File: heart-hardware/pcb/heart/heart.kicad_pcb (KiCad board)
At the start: 4 copper layers, 47.6 x 45.2 mm, 68 parts, among them J1 3V0, J2 DIO, J3 CLK, J4 GND, J5 TOUCH_KEY, SW1 SW_SPDT, U1 STM32L031F6Px, U2 TCA6416APWR, U3 LIS3DH, U4 Holtek-Semicon-BS812A-1

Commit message: Version 1.0
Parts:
- renumbered JP3 to RST
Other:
- board text added: "github/lime7git"
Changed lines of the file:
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@@
   (general
     (thickness 1.6)
-    (drawings 41)
+    (drawings 42)
     (tracks 464)
     (zones 0)
@@
     (1 In1.Cu signal)
     (2 In2.Cu signal)
-    (31 B.Cu signal)
+    (31 B.Cu signal hide)
     (32 B.Adhes user)
     (33 F.Adhes user)
@@
     (tags "solder jumper open")
     (attr virtual)
-    (fp_text reference JP3 (at -2.75 -0.01) (layer B.SilkS)
+    (fp_text reference RST (at -2.75 -0.01) (layer B.SilkS)
       (effects (font (size 1 1) (thickness 0.15)) (justify mirror))
     )
@@
       ))
   )
+  (gr_text github/lime7git (at 50 98) (layer B.SilkS)
+    (effects (font (size 0.5 0.5) (thickness 0.1)) (justify mirror))
+  )
   (gr_arc (start 50.006349 60.288693) (end 52.636348 59.968694) (angle 194.5) (layer B.SilkS) (width 0.2))

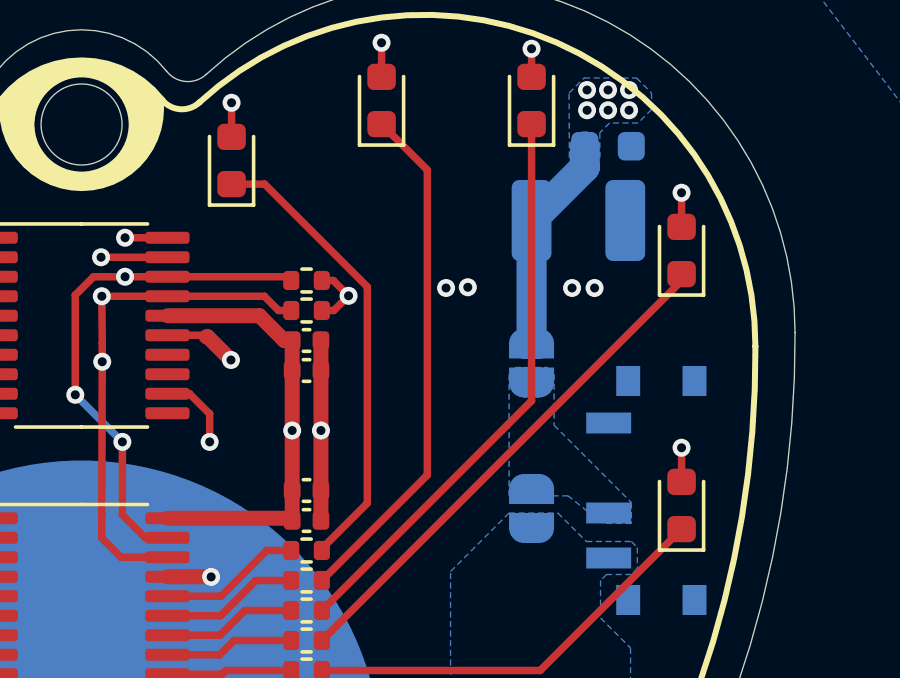
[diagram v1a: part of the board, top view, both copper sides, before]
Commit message: Version 1.01, change power planes clearance
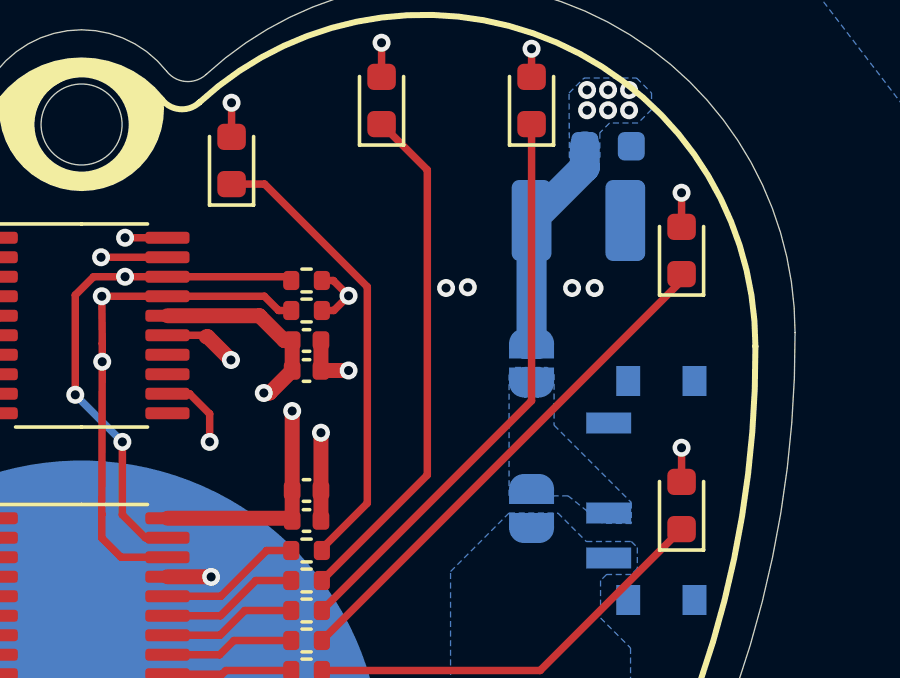
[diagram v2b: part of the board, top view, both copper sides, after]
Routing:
- net GND: track 32.9 -> 31.7 mm, vias 15 -> 16
- net +3V0: track 86.3 -> 86.2 mm, vias 30 -> 31
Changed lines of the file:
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@@
     (thickness 1.6)
     (drawings 42)
-    (tracks 464)
+    (tracks 467)
     (zones 0)
     (modules 68)
@@
     (1 In1.Cu signal)
     (2 In2.Cu signal)
-    (31 B.Cu signal hide)
+    (31 B.Cu signal)
     (32 B.Adhes user)
     (33 F.Adhes user)
@@
     (user_trace_width 1)
     (trace_clearance 0.2)
-    (zone_clearance 0.508)
+    (zone_clearance 0.254)
     (zone_45_only no)
     (trace_min 0.2)
@@
       (outputformat 1)
       (mirror false)
-      (drillshape 1)
+      (drillshape 0)
       (scaleselection 1)
-      (outputdirectory ""))
+      (outputdirectory "../../production-files/"))
   )
   (net 0 "")
@@
       (effects (font (size 1 1) (thickness 0.15)))
     )
-    (fp_text user %R (at 0 0) (layer F.Fab)
-      (effects (font (size 0.75 0.75) (thickness 0.11)))
-    )
     (fp_line (start 0.935 -1.61) (end 1.61 -1.61) (layer F.SilkS) (width 0.12))
     (fp_line (start 1.61 -1.61) (end 1.61 -1.435) (layer F.SilkS) (width 0.12))
@@
     (fp_line (start 1.75 1.75) (end 1.75 -1.75) (layer F.CrtYd) (width 0.05))
     (fp_line (start 1.75 -1.75) (end -1.75 -1.75) (layer F.CrtYd) (width 0.05))
+    (fp_text user %R (at 0 0) (layer F.Fab)
+      (effects (font (size 0.75 0.75) (thickness 0.11)))
+    )
     (pad 16 smd roundrect (at -0.5 -1.225) (size 0.35 0.55) (layers F.Cu F.Paste F.Mask) (roundrect_rratio 0.25)
       (net 37 "Net-(U3-Pad16)"))
@@
       (effects (font (size 0.8 0.8) (thickness 0.12)) (justify mirror))
     )
-    (pad 2 smd roundrect (at 1.5625 0) (size 1.325 2.7) (layers B.Cu B.Paste B.Mask) (roundrect_rratio 0.188679)
+    (pad 2 smd roundrect (at 1.5625 0) (size 1.325 2.7) (layers B.Cu B.Paste B.Mask) (roundrect_rratio 0.1886784905660377)
       (net 2 GND))
-    (pad 1 smd roundrect (at -1.5625 0) (size 1.325 2.7) (layers B.Cu B.Paste B.Mask) (roundrect_rratio 0.188679)
+    (pad 1 smd roundrect (at -1.5625 0) (size 1.325 2.7) (layers B.Cu B.Paste B.Mask) (roundrect_rratio 0.1886784905660377)
       (net 3 +3V0))
     (model ${KISYS3DMOD}/Capacitor_SMD.3dshapes/C_1210_3225Metric.wrl
@@
     (effects (font (size 2.900172 2.610154) (thickness 0.362521)) (justify left top))
   )
+  (via (at 58.9 69) (size 0.6) (drill 0.3) (layers F.Cu B.Cu) (net 2))
+  (via (at 56.075 69.75) (size 0.6) (drill 0.3) (layers F.Cu B.Cu) (net 3))
   (via (at 44.725 85.5) (size 0.6) (drill 0.3) (layers F.Cu B.Cu) (net 2))
-  (via (at 32.175 66.675) (size 0.6) (drill 0.3) (layers F.Cu B.Cu) (net 3))
-  (via (at 66.85 60.325) (size 0.6) (drill 0.3) (layers F.Cu B.Cu) (net 3))
-  (via (at 67.55 60.325) (size 0.6) (drill 0.3) (layers F.Cu B.Cu) (net 3))
-  (via (at 68.25 60.325) (size 0.6) (drill 0.3) (layers F.Cu B.Cu) (net 3))
-  (via (at 68.25 59.65) (size 0.6) (drill 0.3) (layers F.Cu B.Cu) (net 3))
-  (via (at 67.55 59.65) (size 0.6) (drill 0.3) (layers F.Cu B.Cu) (net 3))
-  (via (at 66.85 59.65) (size 0.6) (drill 0.3) (layers F.Cu B.Cu) (net 3))
   (via (at 45.5 81.5) (size 0.6) (drill 0.3) (layers F.Cu B.Cu) (net 2))
   (via (at 54.32 75.88) (size 0.6) (drill 0.3) (layers F.Cu B.Cu) (net 2))
   (via (at 42.02 68.1) (size 0.6) (drill 0.3) (layers F.Cu B.Cu) (net 2))
   (via (at 54.98 68.65) (size 0.6) (drill 0.3) (layers F.Cu B.Cu) (net 2))
-  (via (at 57.98 71) (size 0.6) (drill 0.3) (layers F.Cu B.Cu) (net 2))
+  (via (at 57.98 71.075) (size 0.6) (drill 0.3) (layers F.Cu B.Cu) (net 2))
   (segment (start 52.8675 67.82) (end 52.8625 67.825) (width 0.25) (layer F.Cu) (net 2))
   (segment (start 52.8675 75.88) (end 52.8625 75.875) (width 0.25) (layer F.Cu) (net 2))
@@
   (segment (start 48.775 86) (end 48.775 87.035) (width 0.25) (layer F.Cu) (net 2))
   (segment (start 57.98 68) (end 57.98 69) (width 0.5) (layer F.Cu) (net 2))
-  (segment (start 57.98 71) (end 57.98 69) (width 0.5) (layer F.Cu) (net 2))
-  (segment (start 57.98 71) (end 57.98 73) (width 0.5) (layer F.Cu) (net 2))
   (segment (start 41.99 65.175) (end 41.99 66.145) (width 0.5) (layer F.Cu) (net 2))
   (segment (start 42.02 66.175) (end 41.99 66.145) (width 0.5) (layer F.Cu) (net 2))
@@
   (segment (start 54.20501 67.87501) (end 54.155 67.87501) (width 0.5) (layer F.Cu) (net 2))
   (segment (start 54.98 68.65) (end 54.20501 67.87501) (width 0.5) (layer F.Cu) (net 2))
+  (segment (start 57.98 73) (end 57.98 71.075) (width 0.5) (layer F.Cu) (net 2))
+  (segment (start 58.9 69) (end 57.98 69) (width 0.5) (layer F.Cu) (net 2))
+  (via (at 32.175 66.675) (size 0.6) (drill 0.3) (layers F.Cu B.Cu) (net 3))
+  (via (at 66.85 60.325) (size 0.6) (drill 0.3) (layers F.Cu B.Cu) (net 3))
+  (via (at 67.55 60.325) (size 0.6) (drill 0.3) (layers F.Cu B.Cu) (net 3))
+  (via (at 68.25 60.325) (size 0.6) (drill 0.3) (layers F.Cu B.Cu) (net 3))
+  (via (at 68.25 59.65) (size 0.6) (drill 0.3) (layers F.Cu B.Cu) (net 3))
+  (via (at 67.55 59.65) (size 0.6) (drill 0.3) (layers F.Cu B.Cu) (net 3))
+  (via (at 66.85 59.65) (size 0.6) (drill 0.3) (layers F.Cu B.Cu) (net 3))
   (via (at 55 60.075) (size 0.6) (drill 0.3) (layers F.Cu B.Cu) (net 3))
   (via (at 60 58.075) (size 0.6) (drill 0.3) (layers F.Cu B.Cu) (net 3))
@@
   (via (at 69.25 81.7) (size 0.6) (drill 0.3) (layers F.Cu B.Cu) (net 3))
   (via (at 43.175 68.1) (size 0.6) (drill 0.3) (layers F.Cu B.Cu) (net 3))
-  (via (at 57.02 71) (size 0.6) (drill 0.3) (layers F.Cu B.Cu) (net 3))
+  (via (at 57.02 70.35) (size 0.6) (drill 0.3) (layers F.Cu B.Cu) (net 3))
   (via (at 58.9 66.51) (size 0.6) (drill 0.3) (layers F.Cu B.Cu) (net 3))
   (segment (start 58.39 66) (end 58.9 66.51) (width 0.25) (layer F.Cu) (net 3))
@@
   (segment (start 52.8625 73.925) (end 56.945 73.925) (width 0.5) (layer F.Cu) (net 3))
   (segment (start 57.02 68) (end 57.02 69) (width 0.5) (layer F.Cu) (net 3))
-  (segment (start 57.02 69) (end 57.02 71) (width 0.5) (layer F.Cu) (net 3))
-  (segment (start 57.02 71) (end 57.02 73) (width 0.5) (layer F.Cu) (net 3))
   (segment (start 43.080001 67.074999) (end 42.98 67.175) (width 0.5) (layer F.Cu) (net 3))
   (segment (start 46.035001 67.074999) (end 43.080001 67.074999) (width 0.5) (layer F.Cu) (net 3))
@@
   (segment (start 41.3 89.02) (end 46 89.02) (width 0.5) (layer F.Cu) (net 3))
   (segment (start 45.1575 87.9175) (end 44.0725 89.0025) (width 0.5) (layer F.Cu) (net 3))
+  (segment (start 57.02 73) (end 57.02 70.35) (width 0.5) (layer F.Cu) (net 3))
+  (segment (start 56.27 69.75) (end 57.02 69) (width 0.5) (layer F.Cu) (net 3))
+  (segment (start 56.075 69.75) (end 56.27 69.75) (width 0.5) (layer F.Cu) (net 3))
   (segment (start 43.406946 62.7875) (end 45 62.7875) (width 0.25) (layer F.Cu) (net 4))
   (segment (start 41.394999 64.799447) (end 43.406946 62.7875) (width 0.25) (layer F.Cu) (net 4))
@@
   )
   (zone (net 3) (net_name +3V0) (layer In2.Cu) (hatch full 0.508)
-    (connect_pads yes (clearance 0.508))
+    (connect_pads yes (clearance 0.254))
     (min_thickness 0.254)
     (fill yes (arc_segments 32) (thermal_gap 0.508) (thermal_bridge_width 0.508))

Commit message: Version 1.02
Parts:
- C1: footprint Capacitor_SMD:C_0603_1608Metric -> Capacitor_SMD:C_0402_1005Metric
- R24: value R_Small -> 10k
